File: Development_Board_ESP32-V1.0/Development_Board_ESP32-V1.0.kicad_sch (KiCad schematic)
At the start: 95 parts, among them J1 USB_B, J2 GPIO, J3 OLED, Q1 MMBT3904, Q2 MMBT3904, Q3 MMBT3904, Q4 MMBT3904, Q5 MMBT3904, Q6 MMBT3904, U1 ESP32-WROOM-32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

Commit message: Subiendo todo por si cambio
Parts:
- R5: value 1K -> 470
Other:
- note added: "ANALOG INPUT"
- note added: "BOOT SETTINGS"
- note added: "BUZZER"
- note added: "ESP32-WROOM-32"
- note added: "GPIO - UART"
- note added: "INPUT-OUTPUT DIGITAL"
- note added: "JUMPER SELECTOR"
- note added: "LED WS2812B"
- note added: "MOUNT HOLE"
- note added: "OLED-I2C"
- note added: "POWER SUPPLY"
- note added: "RELAY OUTPUT"
- note added: "USB TO TTL"
- note removed: "GPIO34 GPIO35 GPIO36 GPIO39"
- moved on the sheet: BZ1, C10, C12, C13, C14, C15, C16, C3, C4, C5, C6, C7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

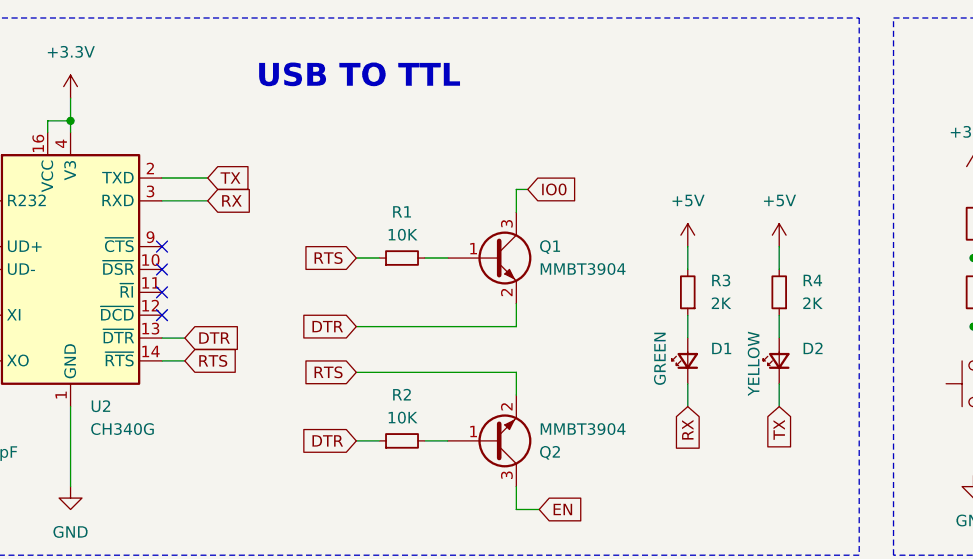
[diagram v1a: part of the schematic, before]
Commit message: Arreglando Voltaje en esquematico
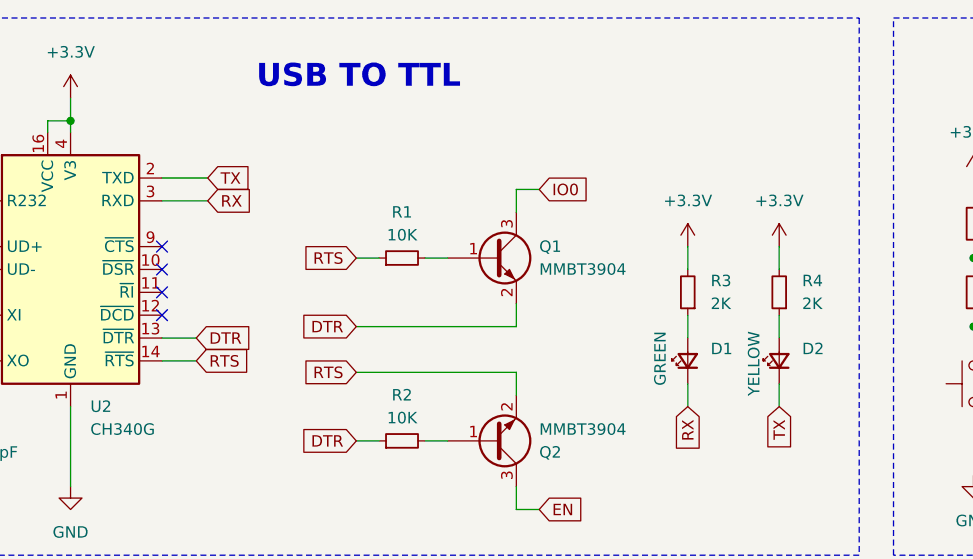
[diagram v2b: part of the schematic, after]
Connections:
- net +3.3V: now also R3.2, R4.2
- net +5V: no longer R3.2, R4.2
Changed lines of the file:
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@@
 	(wire
 		(pts
-			(xy 171.45 57.15) (xy 173.99 57.15)
+			(xy 171.45 57.15) (xy 175.26 57.15)
 		)
 		(stroke
@@
 	(wire
 		(pts
-			(xy 171.45 54.61) (xy 173.99 54.61)
+			(xy 171.45 54.61) (xy 175.26 54.61)
 		)
 		(stroke
@@
 	(wire
 		(pts
-			(xy 212.09 38.1) (xy 210.82 38.1)
+			(xy 213.36 38.1) (xy 210.82 38.1)
 		)
 		(stroke
@@
 	(global_label "IO0"
 		(shape input)
-		(at 212.09 38.1 0)
+		(at 213.36 38.1 0)
 		(fields_autoplaced yes)
 		(effects
@@
 		)
 		(property "Intersheetrefs" "${INTERSHEET_REFS}"
-			(at 218.22 38.1 0)
+			(at 219.49 38.1 0)
 			(effects
 				(font
@@
 	(global_label "DTR"
 		(shape input)
-		(at 173.99 54.61 0)
+		(at 175.26 54.61 0)
 		(fields_autoplaced yes)
 		(effects
@@
 		)
 		(property "Intersheetrefs" "${INTERSHEET_REFS}"
-			(at 180.4828 54.61 0)
+			(at 181.7528 54.61 0)
 			(effects
 				(font
@@
 	(global_label "RTS"
 		(shape input)
-		(at 173.99 57.15 0)
+		(at 175.26 57.15 0)
 		(fields_autoplaced yes)
 		(effects
@@
 		)
 		(property "Intersheetrefs" "${INTERSHEET_REFS}"
-			(at 180.4223 57.15 0)
+			(at 181.6923 57.15 0)
 			(effects
 				(font
@@
 	)
 	(symbol
+		(lib_id "power:+3.3V")
+		(at 240.03 44.45 0)
+		(unit 1)
+		(exclude_from_sim no)
+		(in_bom yes)
+		(on_board yes)
+		(dnp no)
+		(fields_autoplaced yes)
+		(property "Reference" "#PWR08"
+			(at 240.03 48.26 0)
+			(effects
+				(font
+					(size 1.27 1.27)
+				)
+				(hide yes)
+			)
+		)
+		(property "Value" "+3.3V"
+			(at 240.03 39.37 0)
+			(effects
+				(font
+					(size 1.27 1.27)
+				)
+			)
+		)
+		(property "Footprint" ""
+			(at 240.03 44.45 0)
+			(effects
+				(font
+					(size 1.27 1.27)
+				)
+				(hide yes)
+			)
+		)
+		(property "Datasheet" ""
+			(at 240.03 44.45 0)
+			(effects
+				(font
+					(size 1.27 1.27)
+				)
+				(hide yes)
+			)
+		)
+		(property "Description" "Power symbol creates a global label with name \"+3.3V\""
+			(at 240.03 44.45 0)
+			(effects
+				(font
+					(size 1.27 1.27)
+				)
+				(hide yes)
+			)
+		)
+		(pin "1"
+		)
+		(instances
+			(project "Development_Board_ESP32-V1.0"
+				(path "/bfe657c0-e4c3-4a68-802c-828858edf143"
+					(reference "#PWR08")
+					(unit 1)
+				)
+			)
+		)
+	)
+	(symbol
 		(lib_id "power:GND")
 		(at 160.02 116.84 0)
@@
 	(symbol
 		(lib_id "power:+5V")
-		(at 240.03 44.45 0)
-		(unit 1)
-		(exclude_from_sim no)
-		(in_bom yes)
-		(on_board yes)
-		(dnp no)
-		(fields_autoplaced yes)
-		(property "Reference" "#PWR08"
-			(at 240.03 48.26 0)
-			(effects
-				(font
-					(size 1.27 1.27)
-				)
-				(hide yes)
-			)
-		)
-		(property "Value" "+5V"
-			(at 240.03 39.37 0)
-			(effects
-				(font
-					(size 1.27 1.27)
-				)
-			)
-		)
-		(property "Footprint" ""
-			(at 240.03 44.45 0)
-			(effects
-				(font
-					(size 1.27 1.27)
-				)
-				(hide yes)
-			)
-		)
-		(property "Datasheet" ""
-			(at 240.03 44.45 0)
-			(effects
-				(font
-					(size 1.27 1.27)
-				)
-				(hide yes)
-			)
-		)
-		(property "Description" "Power symbol creates a global label with name \"+5V\""
-			(at 240.03 44.45 0)
-			(effects
-				(font
-					(size 1.27 1.27)
-				)
-				(hide yes)
-			)
-		)
-		(pin "1"
-		)
-		(instances
-			(project "Development_Board_ESP32-V1.0"
-				(path "/bfe657c0-e4c3-4a68-802c-828858edf143"
-					(reference "#PWR08")
-					(unit 1)
-				)
-			)
-		)
-	)
-	(symbol
-		(lib_id "power:+5V")
 		(at 96.52 205.74 0)
 		(unit 1)
@@
 	)
 	(symbol
+		(lib_id "power:+3.3V")
+		(at 229.87 44.45 0)
+		(unit 1)
+		(exclude_from_sim no)
+		(in_bom yes)
+		(on_board yes)
+		(dnp no)
+		(fields_autoplaced yes)
+		(property "Reference" "#PWR07"
+			(at 229.87 48.26 0)
+			(effects
+				(font
+					(size 1.27 1.27)
+				)
+				(hide yes)
+			)
+		)
+		(property "Value" "+3.3V"
+			(at 229.87 39.37 0)
+			(effects
+				(font
+					(size 1.27 1.27)
+				)
+			)
+		)
+		(property "Footprint" ""
+			(at 229.87 44.45 0)
+			(effects
+				(font
+					(size 1.27 1.27)
+				)
+				(hide yes)
+			)
+		)
+		(property "Datasheet" ""
+			(at 229.87 44.45 0)
+			(effects
+				(font
+					(size 1.27 1.27)
+				)
+				(hide yes)
+			)
+		)
+		(property "Description" "Power symbol creates a global label with name \"+3.3V\""
+			(at 229.87 44.45 0)
+			(effects
+				(font
+					(size 1.27 1.27)
+				)
+				(hide yes)
+			)
+		)
+		(pin "1"
+		)
+		(instances
+			(project "Development_Board_ESP32-V1.0"
+				(path "/bfe657c0-e4c3-4a68-802c-828858edf143"
+					(reference "#PWR07")
+					(unit 1)
+				)
+			)
+		)
+	)
+	(symbol
 		(lib_id "Device:Buzzer")
 		(at 276.86 100.33 0)
@@
 					(unit 1)
 				)
-			)
-		)
-	)
-	(symbol
-		(lib_id "power:+5V")
-		(at 229.87 44.45 0)
-		(unit 1)
-		(exclude_from_sim no)
-		(in_bom yes)
-		(on_board yes)
-		(dnp no)
-		(fields_autoplaced yes)
-		(property "Reference" "#PWR07"
-			(at 229.87 48.26 0)
-			(effects
-				(font
-					(size 1.27 1.27)
-				)
-				(hide yes)
-			)
-		)
-		(property "Value" "+5V"
-			(at 229.87 39.37 0)
-			(effects
-				(font
-					(size 1.27 1.27)
-				)
-			)
-		)
-		(property "Footprint" ""
-			(at 229.87 44.45 0)
-			(effects
-				(font
-					(size 1.27 1.27)
-				)
-				(hide yes)
-			)
-		)
-		(property "Datasheet" ""
-			(at 229.87 44.45 0)
-			(effects
-				(font
-					(size 1.27 1.27)
-				)
-				(hide yes)
-			)
-		)
-		(property "Description" "Power symbol creates a global label with name \"+5V\""
-			(at 229.87 44.45 0)
-			(effects
-				(font
-					(size 1.27 1.27)
-				)
-				(hide yes)
-			)
-		)
-		(pin "1"
-		)
-		(instances
-			(project ""
-				(path "/bfe657c0-e4c3-4a68-802c-828858edf143"
-					(reference "#PWR07")
-					(unit 1)
-				)
